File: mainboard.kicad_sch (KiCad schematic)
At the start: 22 parts, among them J1 HX711, J10 MainPump, J11 WaterLevelSensor, J12 AuxPump, J13 OneWireTemp, J14 OneWireTemp, J15 FlowSensor, J16 USB_C_Receptacle_USB2.0_16P, J2 Servo, J20 DC 12V IN, J3 Valve1, J4 Valve2, J5 Valve3, J6 Valve4, J7 Valve5, J8 Valve6, J9 Valve7

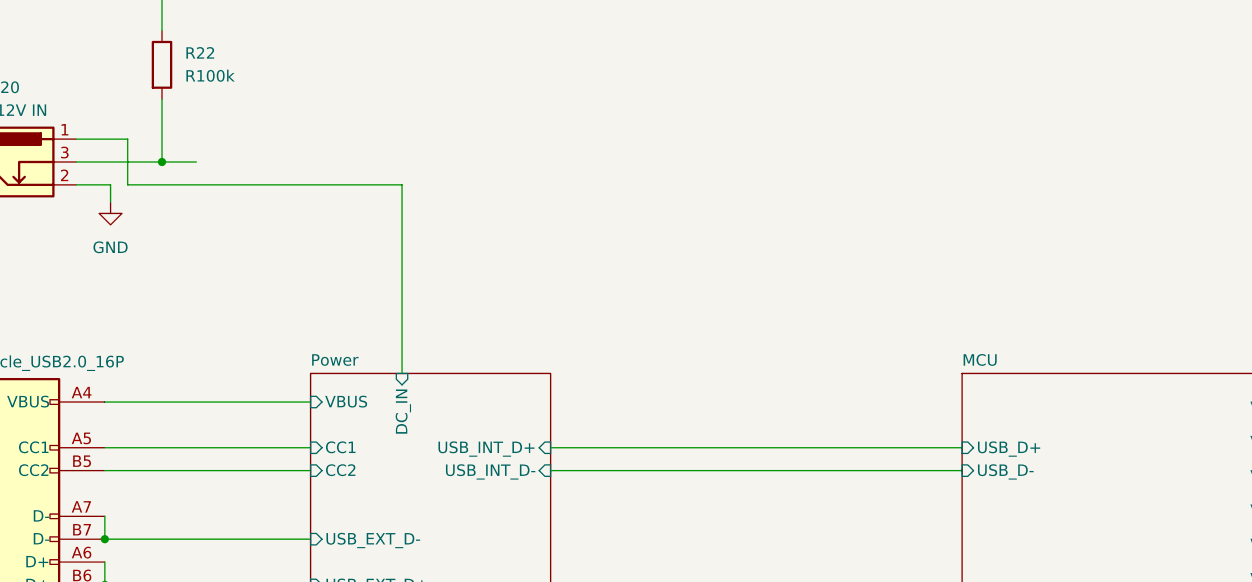
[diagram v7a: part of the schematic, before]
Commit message: Cleanup layout and schematic
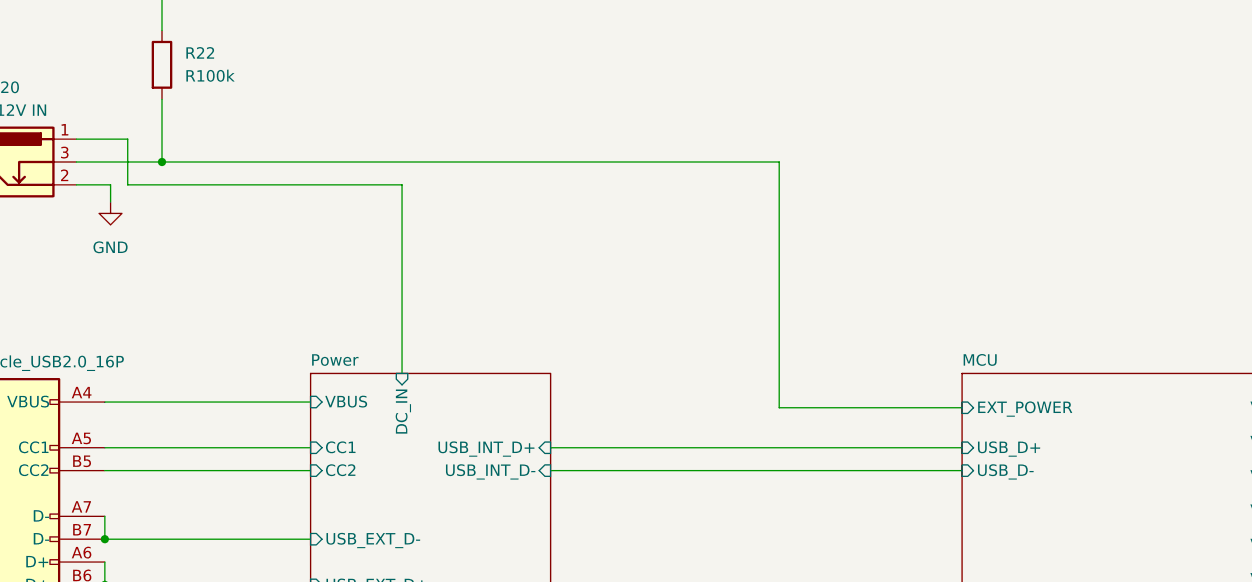
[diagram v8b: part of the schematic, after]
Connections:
- net MCU/EXT_POWER: now reaches J20.3, R22.2
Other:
- sheet MCU ports: added EXT_POWER; removed none
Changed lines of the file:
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@@
     (stroke (width 0) (type default))
   )
-  (wire (pts (xy 88.265 50.165) (xy 92.075 50.165))
+  (wire (pts (xy 88.265 50.165) (xy 156.845 50.165))
+    (stroke (width 0) (type default))
+  )
+  (wire (pts (xy 156.845 77.47) (xy 177.165 77.47))
     (stroke (width 0) (type default))
   )
@@
   )
   (wire (pts (xy 266.7 144.78) (xy 272.415 144.78))
+    (stroke (width 0) (type default))
+  )
+  (wire (pts (xy 156.845 50.165) (xy 156.845 77.47))
     (stroke (width 0) (type default))
   )
@@
       (effects (font (size 1.27 1.27)) (justify left))
     )
+    (pin "EXT_POWER" input (at 177.165 77.47 180)
+      (effects (font (size 1.27 1.27)) (justify left))
+    )
